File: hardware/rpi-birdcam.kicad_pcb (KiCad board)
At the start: 2 copper layers, 104 x 96 mm, 81 parts, among them J101 Conn_01x02, J102 RPI, J103 LTE Cat.1 Pi HAT, Q101 BC847C, Q102 BC847C, Q103 BC847C, Q104 BC847C, Q105 Q_NPN_BEC, SW101 SW_Push, U101 LM393, U102 MCP3204, U103 LM4120, U104 MIC4690, U105 PCF8563, Y101 32.768 kHz

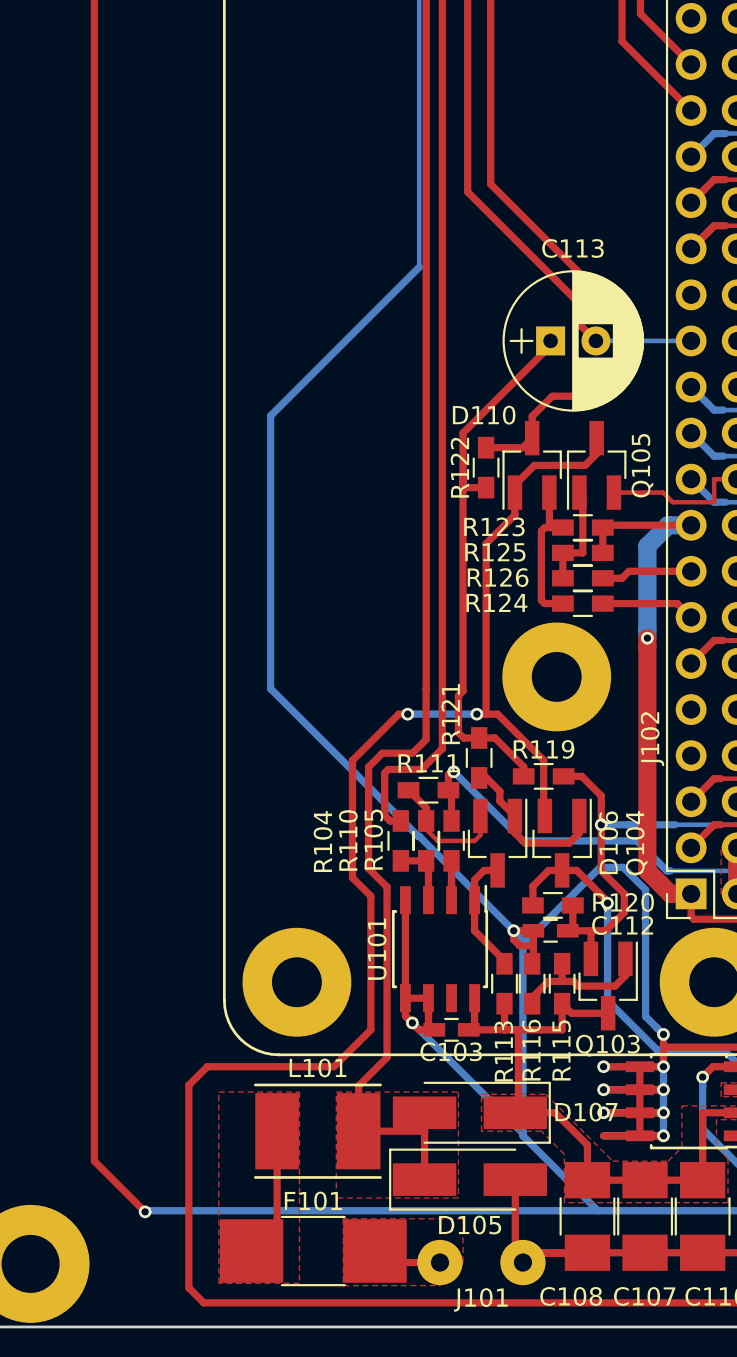
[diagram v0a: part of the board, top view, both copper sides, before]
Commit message: Add text & copyright notice
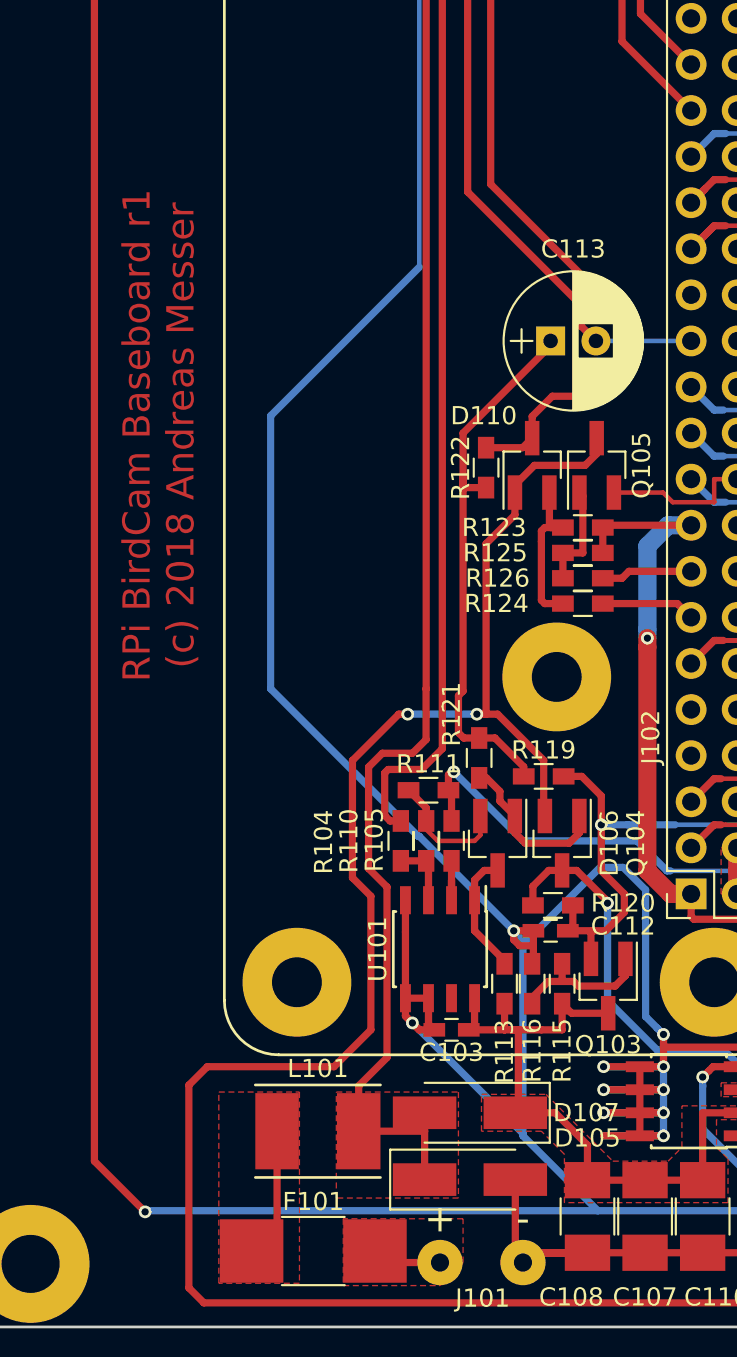
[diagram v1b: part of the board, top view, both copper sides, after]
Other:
- board text added: "+"
- board text added: "-"
- board text added: "RPi BirdCam Baseboard r1 (c) 2018 Andreas Messer"
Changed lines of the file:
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@@
     (area 27.074999 35.574999 135.925001 153.425001)
     (thickness 1.6)
-    (drawings 12)
+    (drawings 15)
     (tracks 1216)
     (zones 0)
@@
     (tags "Diode SMA (DO-214AC) Handsoldering")
     (attr smd)
-    (fp_text reference D105 (at 0 2.54 180) (layer F.SilkS)
+    (fp_text reference D105 (at 6.477 -2.286 180) (layer F.SilkS)
       (effects (font (size 1 1) (thickness 0.15)))
     )
@@
     )
   )
+  (gr_text "RPi BirdCam Baseboard r1\n(c) 2018 Andreas Messer" (at 40.098 93.357 90) (layer F.Cu)
+    (effects (font (size 1.5 1.5) (thickness 0.3)))
+  )
+  (gr_text + (at 55.592 136.537) (layer F.SilkS)
+    (effects (font (size 1.5 1.5) (thickness 0.3)))
+  )
+  (gr_text - (at 60.164 136.537) (layer F.SilkS)
+    (effects (font (size 1.5 1.5) (thickness 0.3)))
+  )
   (gr_line (start 103.725 94.5) (end 91.255 116.098) (layer Dwgs.User) (width 0.2))

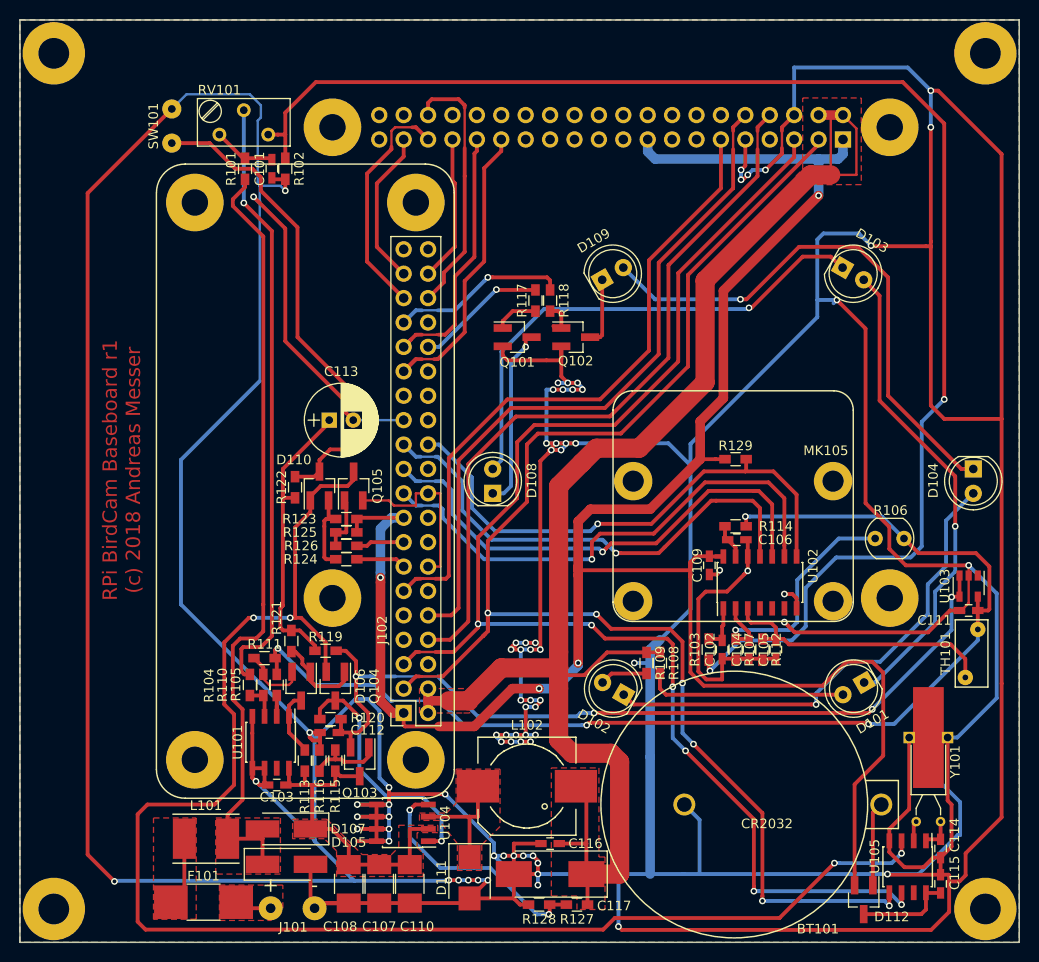
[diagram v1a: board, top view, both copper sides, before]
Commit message: Add meta information & reduce board size
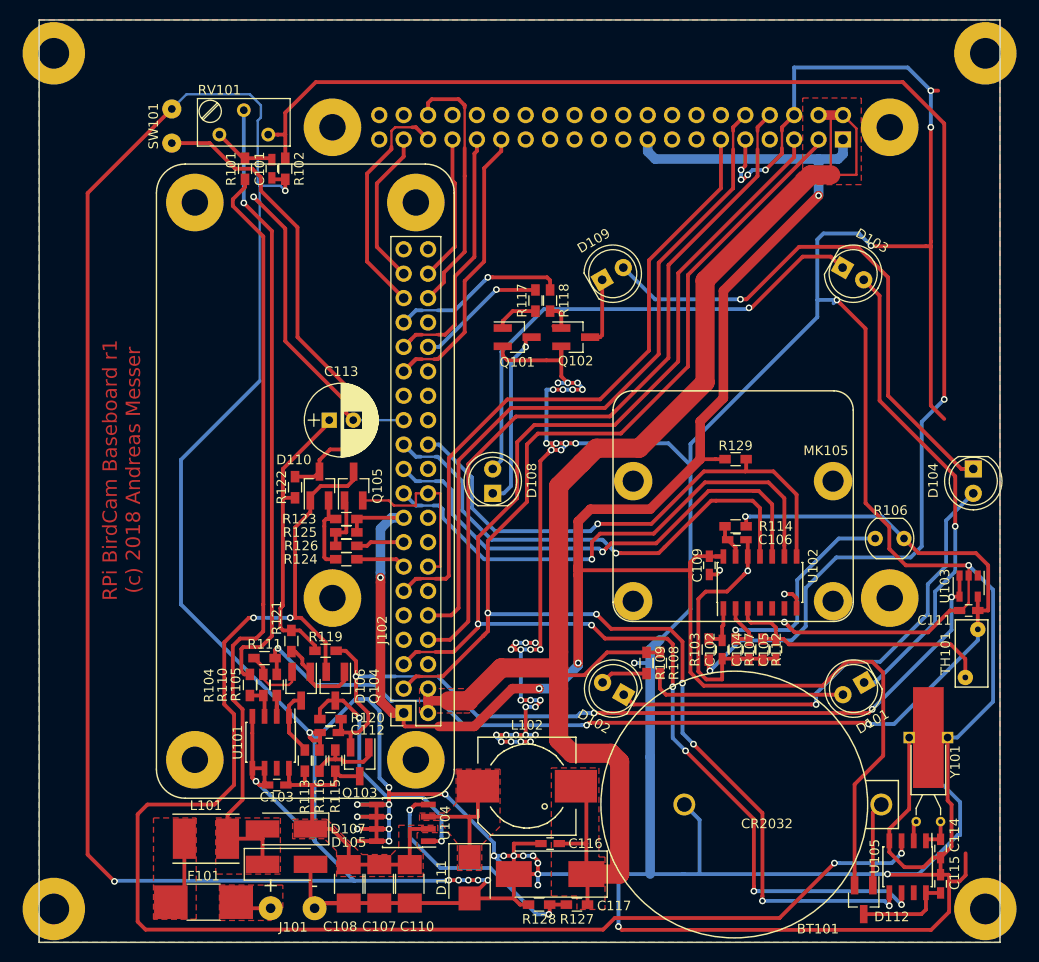
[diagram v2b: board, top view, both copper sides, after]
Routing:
- net GND: track 1060.2 -> 970.2 mm
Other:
- board size 104 x 96 mm -> 100 x 96 mm
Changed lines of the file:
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@@
     (thickness 1.6)
     (drawings 15)
-    (tracks 1216)
+    (tracks 1209)
     (zones 0)
     (modules 81)
@@
     (user_trace_width 2)
     (trace_clearance 0.25)
-    (zone_clearance 0.4)
+    (zone_clearance 0.3)
     (zone_45_only yes)
     (trace_min 0.25)
@@
     (visible_elements FFFE7F7F)
     (pcbplotparams
-      (layerselection 0x00000_80000001)
-      (usegerberextensions false)
-      (excludeedgelayer false)
-      (linewidth 0.050000)
+      (layerselection 0x010f0_80000001)
+      (usegerberextensions true)
+      (excludeedgelayer true)
+      (linewidth 0.100000)
       (plotframeref false)
       (viasonmask false)
@@
       (psa4output false)
       (plotreference true)
-      (plotvalue true)
+      (plotvalue false)
       (plotinvisibletext false)
       (padsonsilk false)
       (subtractmaskfromsilk false)
-      (outputformat 5)
+      (outputformat 1)
       (mirror false)
-      (drillshape 2)
+      (drillshape 0)
       (scaleselection 1)
-      (outputdirectory /tmp))
+      (outputdirectory "/home/andi/Dokumente/Bestellungen/2018-12-29 Elecrow/Gerber/"))
   )
   (net 0 "")
@@
   (gr_line (start 81.5 92.5) (end 81.5 96.5) (layer Dwgs.User) (width 0.2))
   (gr_line (start 79 94.5) (end 84 94.5) (layer Dwgs.User) (width 0.2))
-  (gr_line (start 29.5 142.5) (end 29.5 46.5) (layer Edge.Cuts) (width 0.15))
-  (gr_line (start 133.5 142.5) (end 29.5 142.5) (layer Edge.Cuts) (width 0.15))
-  (gr_line (start 133.5 46.5) (end 133.5 142.5) (layer Edge.Cuts) (width 0.15))
-  (gr_line (start 29.5 46.5) (end 133.5 46.5) (layer Edge.Cuts) (width 0.15))
+  (gr_line (start 31.5 142.5) (end 31.5 46.5) (layer Edge.Cuts) (width 0.15))
+  (gr_line (start 131.5 142.5) (end 31.5 142.5) (layer Edge.Cuts) (width 0.15))
+  (gr_line (start 131.5 46.5) (end 131.5 142.5) (layer Edge.Cuts) (width 0.15))
+  (gr_line (start 31.5 46.5) (end 131.5 46.5) (layer Edge.Cuts) (width 0.15))
   (segment (start 119.145 128.155) (end 119.092 128.155) (width 0.4) (layer F.Cu) (net 1))
   (segment (start 119.092 128.155) (end 118.264 128.983) (width 0.4) (layer F.Cu) (net 1))
   (segment (start 118.264 128.983) (end 118.264 136.561) (width 0.4) (layer F.Cu) (net 1))
+  (segment (start 126.045 121.183) (end 127.045 121.183) (width 0.4) (layer B.Cu) (net 2))
+  (segment (start 127.045 121.183) (end 130.776 117.452) (width 0.4) (layer B.Cu) (net 2))
+  (segment (start 130.776 117.452) (end 130.776 105.803) (width 0.4) (layer B.Cu) (net 2))
+  (segment (start 130.776 105.803) (end 128.236 103.263) (width 0.4) (layer B.Cu) (net 2))
   (segment (start 95.089 113.423) (end 95.089 112.026) (width 1) (layer B.Cu) (net 2))
   (segment (start 95.089 123.202) (end 95.089 113.423) (width 1) (layer B.Cu) (net 2))
@@
   (segment (start 127.2835 136.156) (end 126.204 136.156) (width 0.4) (layer F.Cu) (net 2))
   (segment (start 127.9185 133.235) (end 127.9185 135.521) (width 0.4) (layer F.Cu) (net 2))
-  (segment (start 131.665 129.4885) (end 127.9185 133.235) (width 0.4) (layer F.Cu) (net 2))
-  (segment (start 131.665 115.563) (end 131.665 129.4885) (width 0.4) (layer F.Cu) (net 2))
   (segment (start 105.249 103.834508) (end 104.899001 104.184507) (width 0.4) (layer F.Cu) (net 2))
   (segment (start 104.899001 104.184507) (end 104.896493 104.184507) (width 0.4) (layer F.Cu) (net 2))
@@
   (segment (start 110.075 51.447) (end 110.075 56.4) (width 0.4) (layer B.Cu) (net 2))
   (segment (start 124.299 53.86) (end 125.061 53.86) (width 0.4) (layer F.Cu) (net 2))
-  (segment (start 125.061 53.86) (end 131.665 60.464) (width 0.4) (layer F.Cu) (net 2))
-  (segment (start 131.665 60.464) (end 131.665 88.023) (width 0.4) (layer F.Cu) (net 2))
   (segment (start 124.299 53.86) (end 124.299 57.67) (width 0.4) (layer B.Cu) (net 2))
   (via (at 124.299 57.67) (size 0.7) (drill 0.4) (layers F.Cu B.Cu) (net 2))
-  (segment (start 125.696 88.023) (end 131.665 88.023) (width 0.4) (layer F.Cu) (net 2))
   (segment (start 124.299 86.626) (end 125.696 88.023) (width 0.4) (layer F.Cu) (net 2))
-  (segment (start 131.665 88.023) (end 131.665 115.563) (width 0.4) (layer F.Cu) (net 2))
   (segment (start 95.089 123.202) (end 95.089 135.394) (width 1) (layer B.Cu) (net 2))
   (segment (start 96.105 111.01) (end 99.28 107.835) (width 0.4) (layer B.Cu) (net 2))
@@
   (segment (start 125.315 133.677) (end 124.54 133.677) (width 0.4) (layer F.Cu) (net 2))
   (segment (start 99.28 107.835) (end 99.28 92.849) (width 0.4) (layer B.Cu) (net 2))
-  (segment (start 131.157 117.071) (end 131.157 106.184) (width 0.4) (layer B.Cu) (net 2))
-  (segment (start 131.157 106.184) (end 128.236 103.263) (width 0.4) (layer B.Cu) (net 2))
-  (segment (start 126.045 121.183) (end 127.045 121.183) (width 0.4) (layer B.Cu) (net 2))
-  (segment (start 127.045 121.183) (end 131.157 117.071) (width 0.4) (layer B.Cu) (net 2))
   (segment (start 105.249 102.341) (end 105.249 100.789) (width 0.4) (layer F.Cu) (net 2))
   (segment (start 105.249 100.789) (end 105.056 100.596) (width 0.4) (layer F.Cu) (net 2))
@@
   (segment (start 64.566 99.834) (end 64.566 98.437) (width 0.4) (layer F.Cu) (net 9))
   (segment (start 64.693 98.31) (end 64.566 98.437) (width 0.25) (layer F.Cu) (net 9))
+  (segment (start 121.505 100.469) (end 123.029 101.993) (width 0.4) (layer F.Cu) (net 10))
+  (segment (start 123.029 101.993) (end 128.998 101.993) (width 0.4) (layer F.Cu) (net 10))
+  (segment (start 130.268 107.962) (end 129.186 107.962) (width 0.4) (layer F.Cu) (net 10))
+  (segment (start 128.998 101.993) (end 130.268 103.263) (width 0.4) (layer F.Cu) (net 10))
+  (segment (start 130.268 103.263) (end 130.268 107.962) (width 0.4) (layer F.Cu) (net 10))
   (segment (start 129.1885 111.06187) (end 120.60437 119.646) (width 0.4) (layer B.Cu) (net 10))
   (segment (start 117.822008 119.773) (end 120.47737 119.773) (width 0.4) (layer B.Cu) (net 10))
@@
   (segment (start 56.057 112.065) (end 56.223 111.899) (width 0.4) (layer F.Cu) (net 10))
   (via (at 56.354 111.899) (size 0.7) (drill 0.4) (layers F.Cu B.Cu) (net 10))
-  (segment (start 121.505 100.469) (end 123.029 101.993) (width 0.4) (layer F.Cu) (net 10))
-  (segment (start 123.029 101.993) (end 128.998 101.993) (width 0.4) (layer F.Cu) (net 10))
-  (segment (start 128.998 101.993) (end 130.395 103.39) (width 0.4) (layer F.Cu) (net 10))
-  (segment (start 130.395 103.39) (end 130.395 107.835) (width 0.4) (layer F.Cu) (net 10))
-  (segment (start 130.395 107.835) (end 130.268 107.962) (width 0.4) (layer F.Cu) (net 10))
-  (segment (start 130.268 107.962) (end 129.186 107.962) (width 0.4) (layer F.Cu) (net 10))
   (segment (start 105.079 99.199) (end 105.079 98.266992) (width 0.4) (layer F.Cu) (net 10))
   (segment (start 105.079 98.266992) (end 104.995008 98.183) (width 0.4) (layer F.Cu) (net 10))
@@
   (segment (start 74.769 70.116) (end 71.975 72.91) (width 0.4) (layer F.Cu) (net 63))
   (zone (net 2) (net_name GND) (layer B.Cu) (hatch edge 0.508)
-    (connect_pads (clearance 0.25))
-    (min_thickness 0.25)
+    (connect_pads (clearance 0.3))
+    (min_thickness 0.2)
     (fill yes (arc_segments 32) (thermal_gap 0.3) (thermal_bridge_width 0.4))
     (polygon
       (pts
-        (xy 29.5 46.5) (xy 133.5 46.5) (xy 133.5 142.5) (xy 29.5 142.5)
+        (xy 31.5 46.5) (xy 131.5 46.5) (xy 131.5 142.5) (xy 31.5 142.5)
       )
     )
   )
   (zone (net 2) (net_name GND) (layer F.Cu) (hatch edge 0.508)
-    (connect_pads (clearance 0.25))
-    (min_thickness 0.25)
+    (connect_pads (clearance 0.3))
+    (min_thickness 0.2)
     (fill yes (arc_segments 32) (thermal_gap 0.3) (thermal_bridge_width 0.4))
     (polygon
       (pts
-        (xy 133.5 142.5) (xy 29.5 142.5) (xy 29.5 46.5) (xy 133.5 46.5)
+        (xy 131.5 142.5) (xy 31.5 142.5) (xy 31.5 46.5) (xy 131.5 46.5)
       )
     )

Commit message: Increase via size
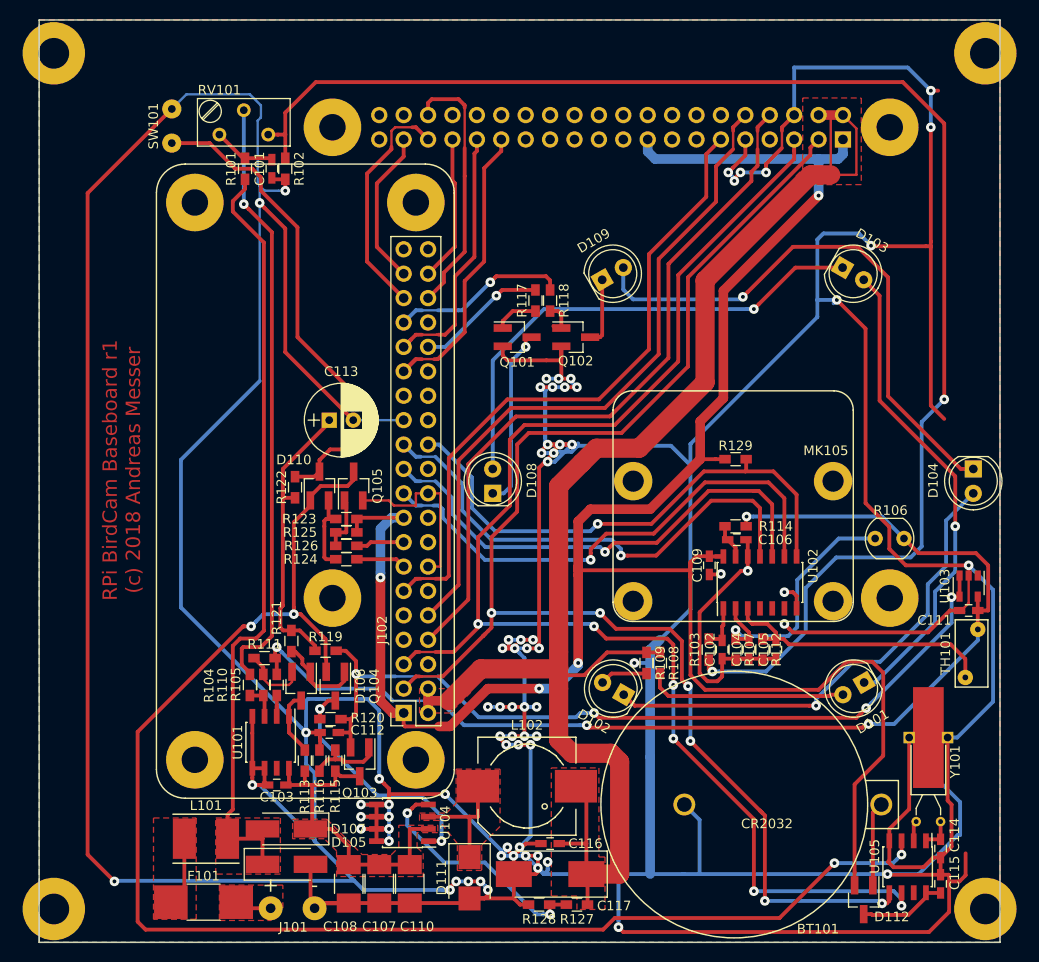
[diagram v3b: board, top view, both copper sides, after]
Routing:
- net GND: track 970.2 -> 997.7 mm, vias 77 -> 75
- net /~PWR_ON~: track 157.8 -> 152.4 mm
- net Net-(C112-Pad1): track 92.7 -> 88.1 mm
- net /RPI_SDA: track 150.7 -> 148.7 mm
- net /LTE_RXD: track 72.9 -> 71.5 mm
- net Net-(D104-Pad1): track 57.2 -> 58.6 mm
- net /LTE_TXD: track 76.4 -> 75.1 mm
- net /RPI_SCL: track 146.2 -> 147.4 mm
- net Net-(D103-Pad1): track 52.7 -> 51.7 mm
- net /~PWR_EN~: track 26.0 -> 26.8 mm
- net Net-(C104-Pad2): track 27.3 -> 28.2 mm
- net Net-(D105-Pad1): track 81.1 -> 80.3 mm
- net Net-(C115-Pad1): track 9.96 -> 9.28 mm
- net /3.3V: track 239.1 -> 239.6 mm
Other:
- net class Default: via_dia 0.7 -> 1
- net class Thicker: via_dia 0.7 -> 1
- rule via_min_size: 0.7 -> 1

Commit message: Fix areas in various places
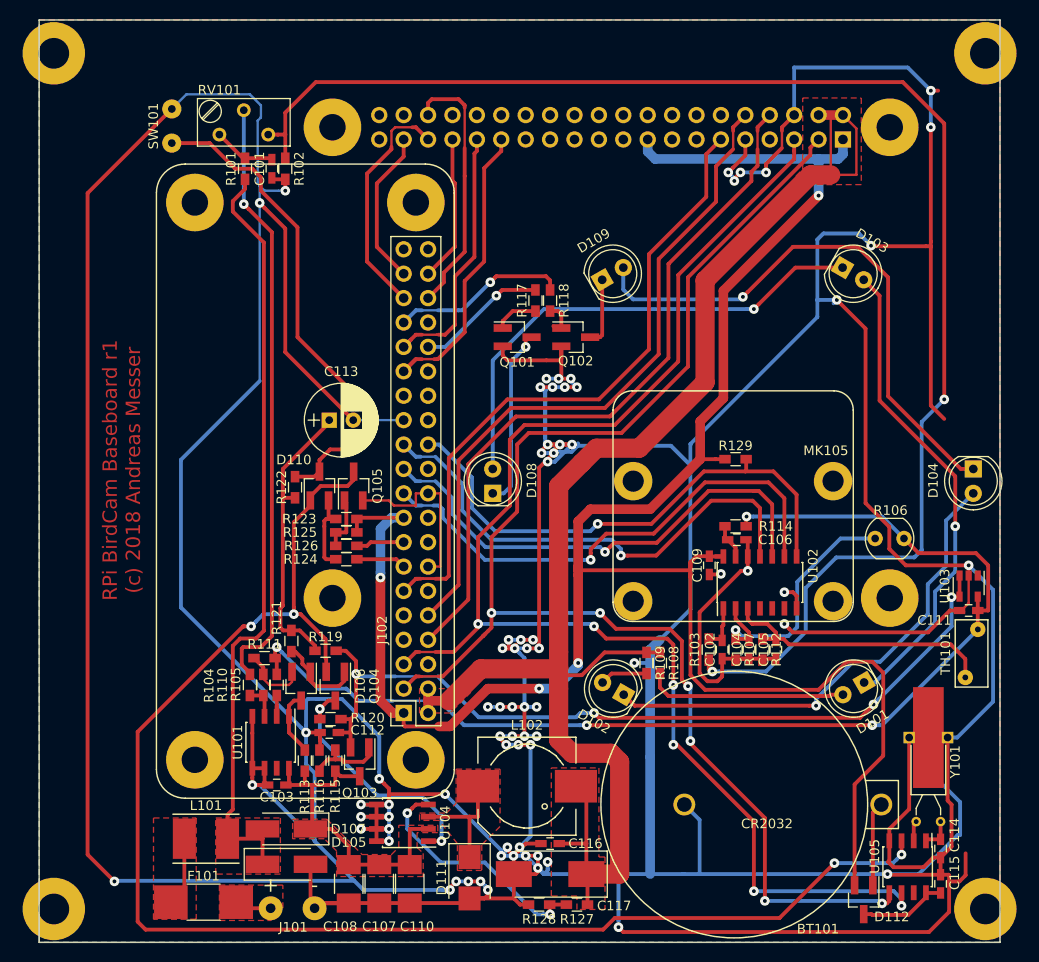
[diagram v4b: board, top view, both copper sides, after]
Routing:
- net GND: track 997.7 -> 996.1 mm
- net /VREF_2.5V: track 122.5 -> 121.3 mm
